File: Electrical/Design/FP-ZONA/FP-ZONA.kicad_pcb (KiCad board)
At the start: 2 copper layers, 105.6 x 105.6 mm, 1 part

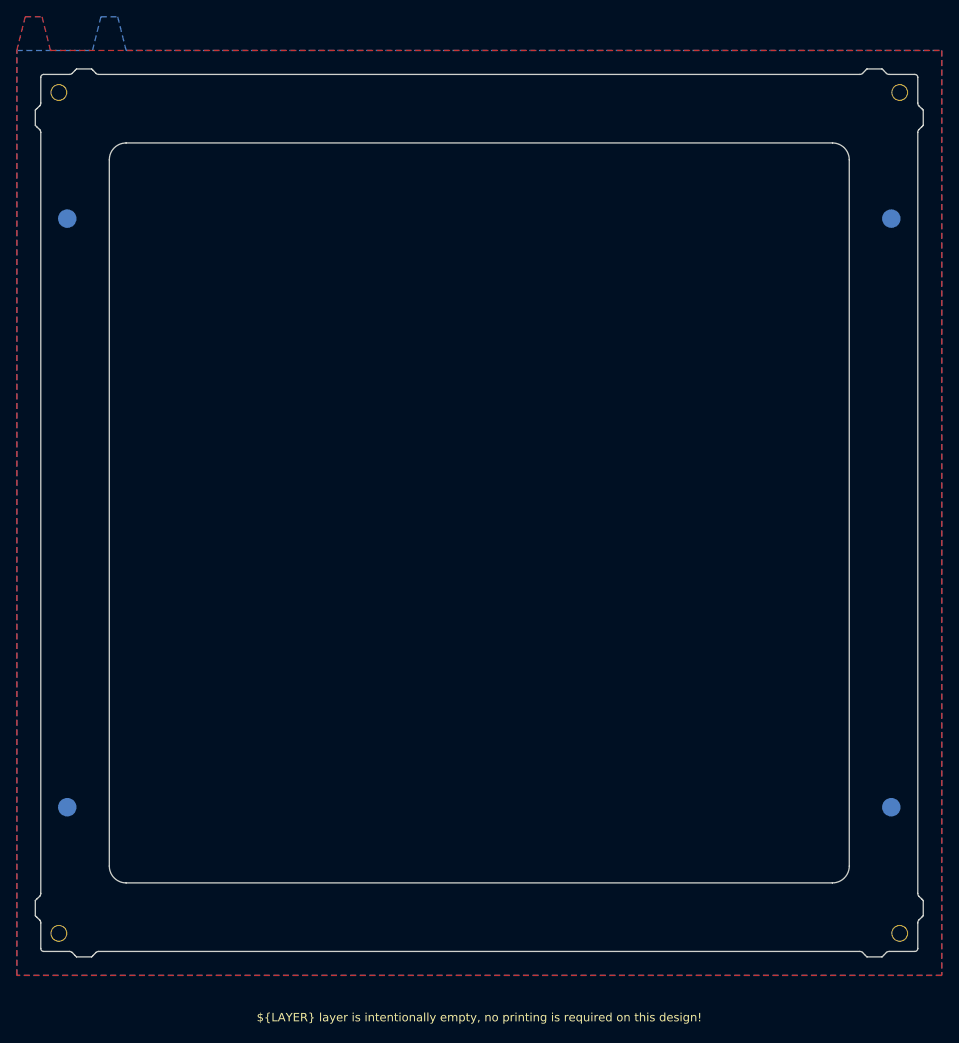
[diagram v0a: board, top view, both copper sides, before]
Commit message: BENB rework zona led/touch dimensions
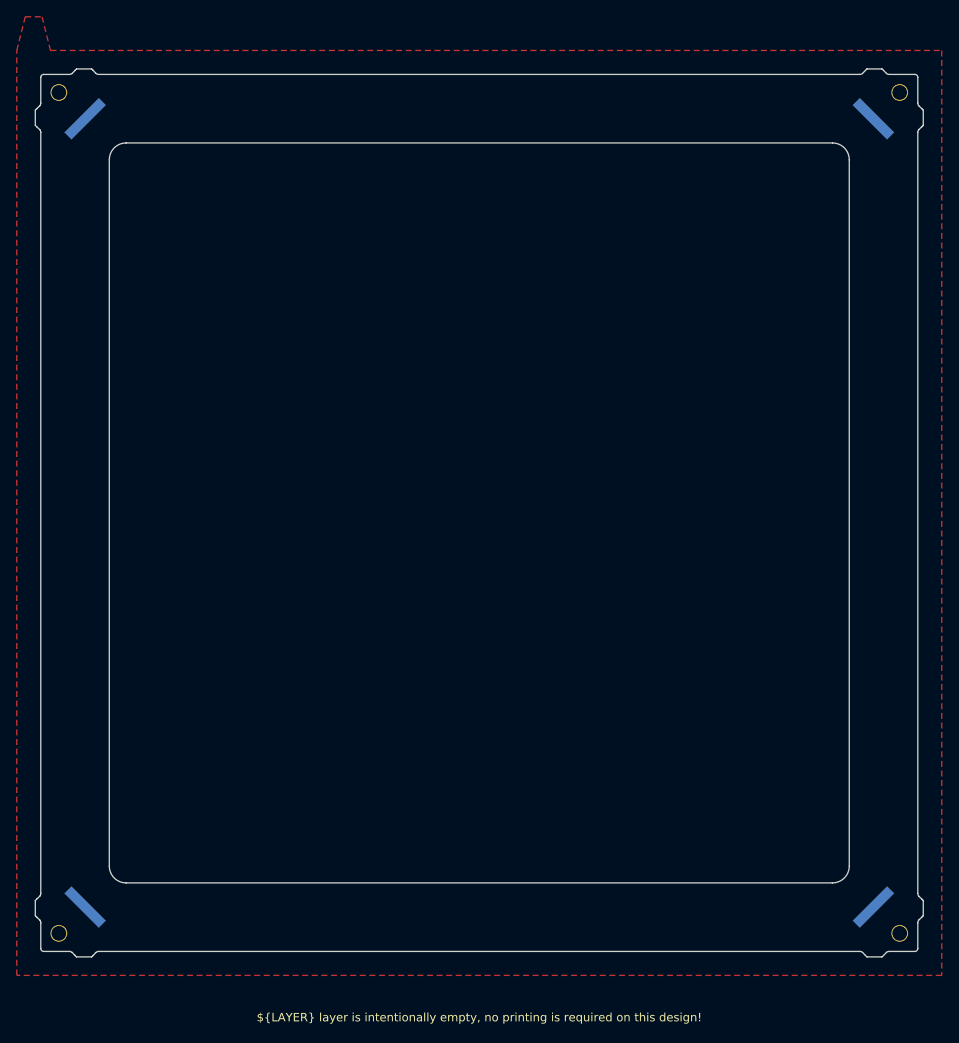
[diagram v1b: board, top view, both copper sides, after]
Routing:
- removed copper zone on B.Cu, net GND
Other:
- board text removed: "SHLD"

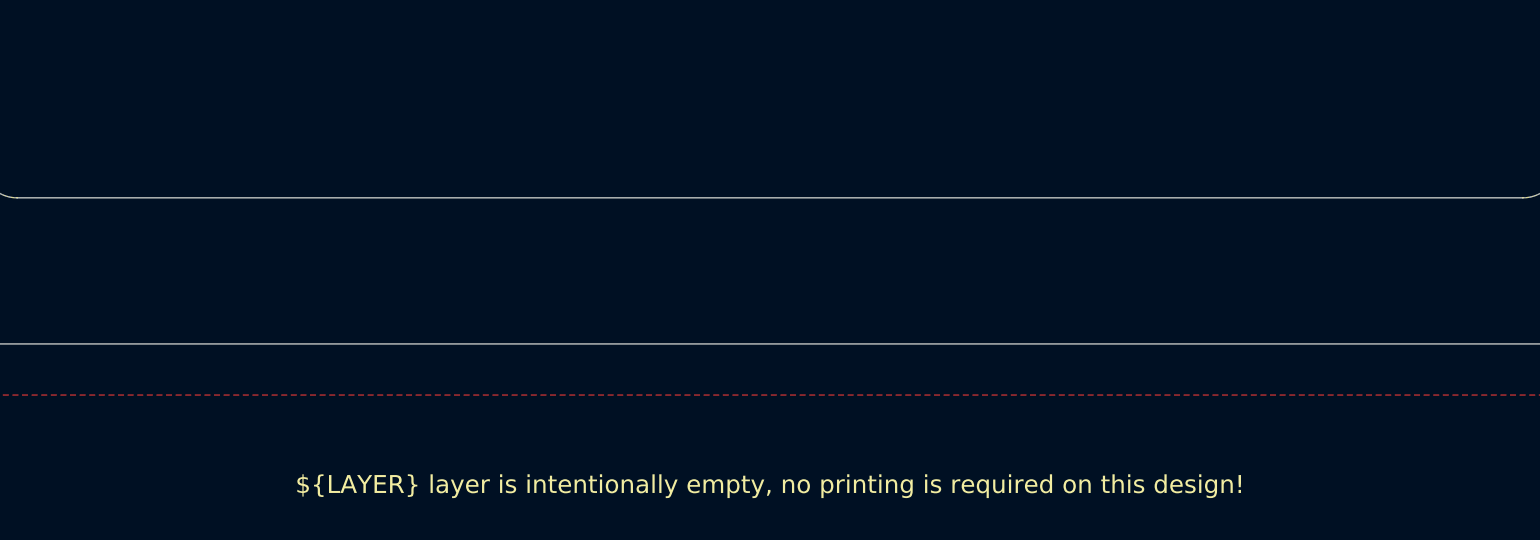
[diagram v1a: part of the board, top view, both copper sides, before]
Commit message: SUKU zones optimized
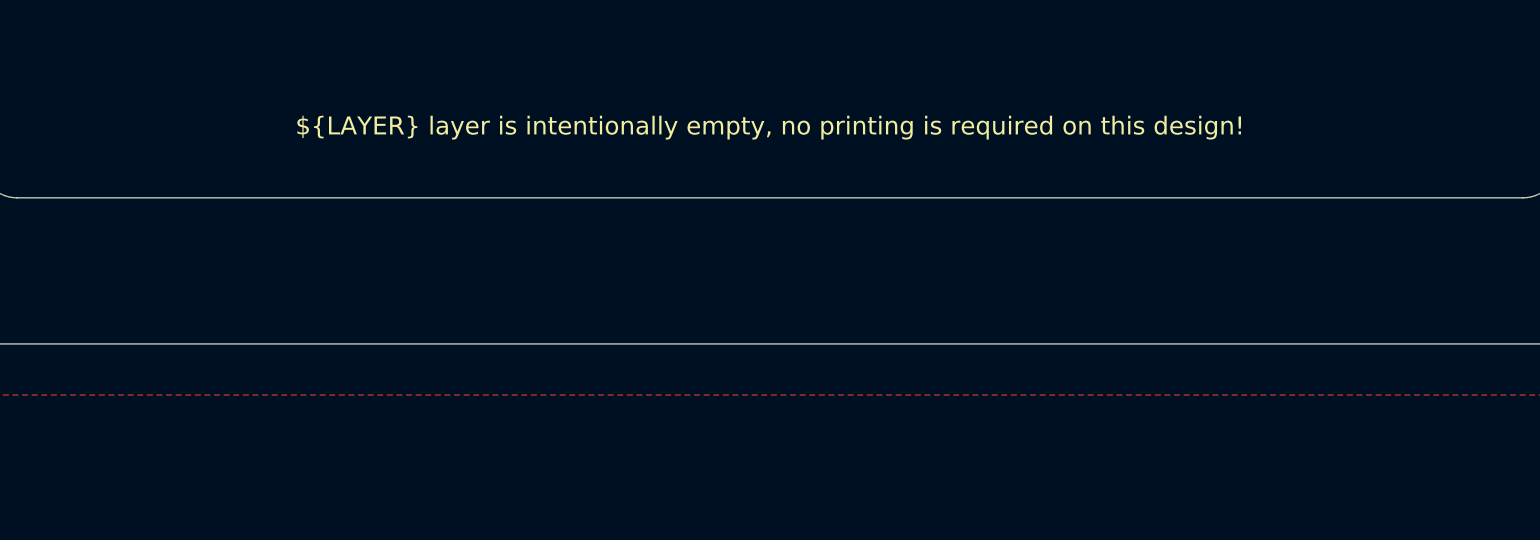
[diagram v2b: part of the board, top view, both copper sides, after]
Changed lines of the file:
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@@
 		(capping no)
 		(filling no)
-		(zone_defaults)
 		(aux_axis_origin 100 100)
 		(grid_origin 100 100)
@@
 	)
 	(gr_text "${LAYER} layer is intentionally empty, no printing is required on this design!"
-		(at 100 160 0)
+		(at 100 140 0)
 		(layer "F.SilkS")
 		(effects
